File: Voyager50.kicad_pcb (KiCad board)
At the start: 2 copper layers, 282.6 x 76.2 mm, 193 parts, among them Q1 2N7002, SW1 SW_Push, U1 ATmega32U2-MU, U2 PRTR5V0U2X, Y1 16Mhz

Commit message: Update readme
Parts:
- added G***: LOGO, locallib:ai-ring-6mm, B.Cu at (92.9, 68.3)
- added G***: LOGO, locallib:ai-ring-6mm, F.Cu at (271.5, 87.3)
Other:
- board text added: "50"
- board text added: "VOYAGER"
- board text added: "Voyager50 PCB Rev 1.0 20190524"
- board text added: "kb.ai03.me"

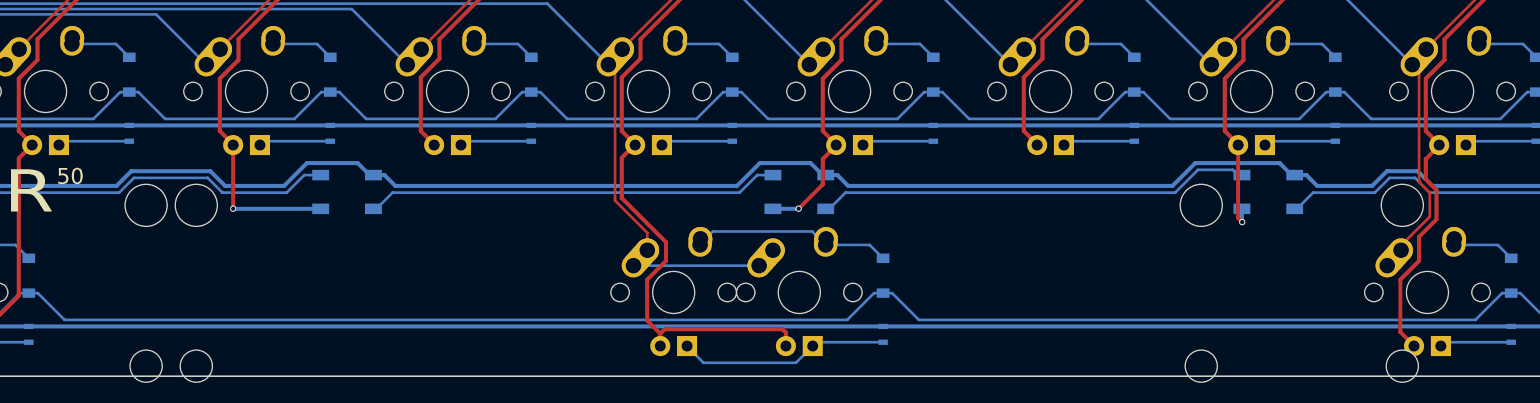
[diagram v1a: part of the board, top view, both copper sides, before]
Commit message: Add split space
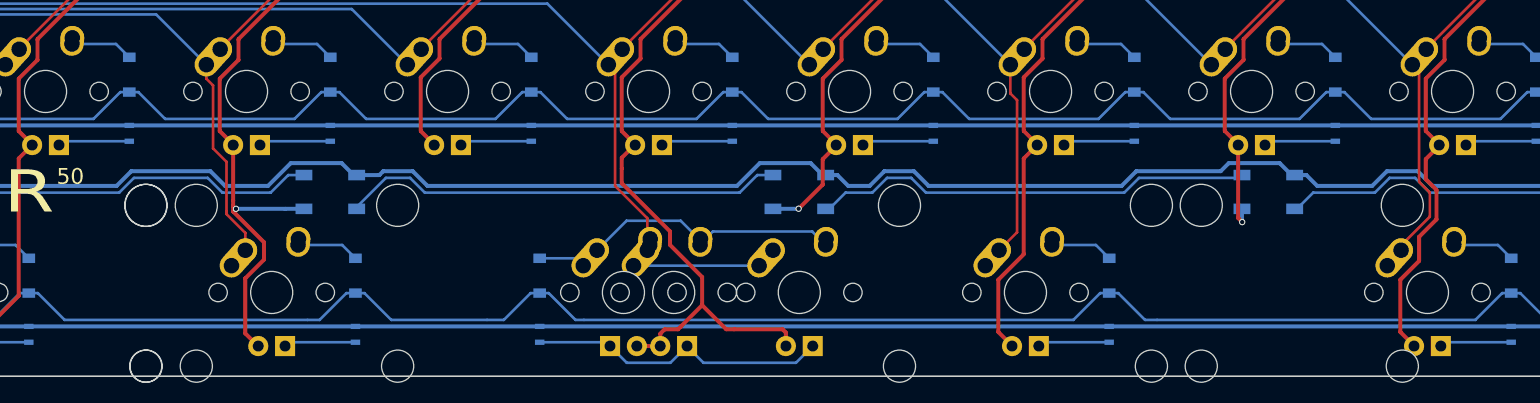
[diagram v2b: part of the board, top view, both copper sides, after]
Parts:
- added D8: SOD-123, Diodes_SMD:D_SOD-123, B.Cu at (134.1, 95.2)
- added D9: SOD-123, Diodes_SMD:D_SOD-123, B.Cu at (205.6, 95.2)
- added K_SPLSPACE1: MX-2.25U, MX_Alps_Hybrid:MX-2.25U-ReversedStabilizers, F.Cu at (126.2, 96.8)
- added K_SPLSPACE2: MX-1.25U, MX_Alps_Hybrid:MX-1.25U-FLIPPED, F.Cu at (159.5, 96.8)
- added K_SPLSPACE3: MX-2.75U, MX_Alps_Hybrid:MX-2.75U-ReversedStabilizers, F.Cu at (197.6, 96.8)
- added R8: 1k, Resistors_SMD:R_0603, B.Cu at (134.1, 100.8)
- added R9: 1k, Resistors_SMD:R_0603, B.Cu at (205.6, 100.8)
- moved D61 32.5 mm to (151.6, 95.2)
- moved R61 32.5 mm to (151.6, 100.8)
- moved RGB10 1.59 mm to (131.8, 87.3)
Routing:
- net +5V: track 1382.8 -> 1419.6 mm
- net COL4: track 105.3 -> 124.4 mm
- net COL8: track 178.9 -> 197.5 mm
- net Net-(D61-Pad2): track 19.0 -> 29.6 mm
- net Net-(K_SPACE1-Pad4): track 20.1 -> 28.7 mm
- net Net-(K_SPLSPACE3-Pad4): track 0.00 -> 6.82 mm
- net Net-(K_SPLSPACE1-Pad4): track 0.00 -> 6.82 mm
- net Net-(D9-Pad2): track 0.00 -> 5.96 mm
- net Net-(D8-Pad2): track 0.00 -> 5.96 mm
- net ROW3: track 300.2 -> 304.4 mm
- net Net-(RGB10-Pad4): track 39.2 -> 42.0 mm
- net Net-(RGB10-Pad2): track 40.3 -> 38.8 mm
- net GND: track 729.8 -> 731.3 mm
- net Net-(RGB6-Pad2): track 41.2 -> 41.9 mm
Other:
- board text added: "Voyager50 PCB Rev 1.1 20190525"
- board text removed: "Voyager50 PCB Rev 1.0 20190524"
